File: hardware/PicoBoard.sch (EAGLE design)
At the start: 44 parts, among them J1 AVR Prog., U1 FT232RLSSOP, U10 SLIDER, U2 ATMEGA328, U3 2.5mm, U4 2.5mm, U5 2.5mm, U6 2.5mm, U7 TEMT6000, U8 LMV358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

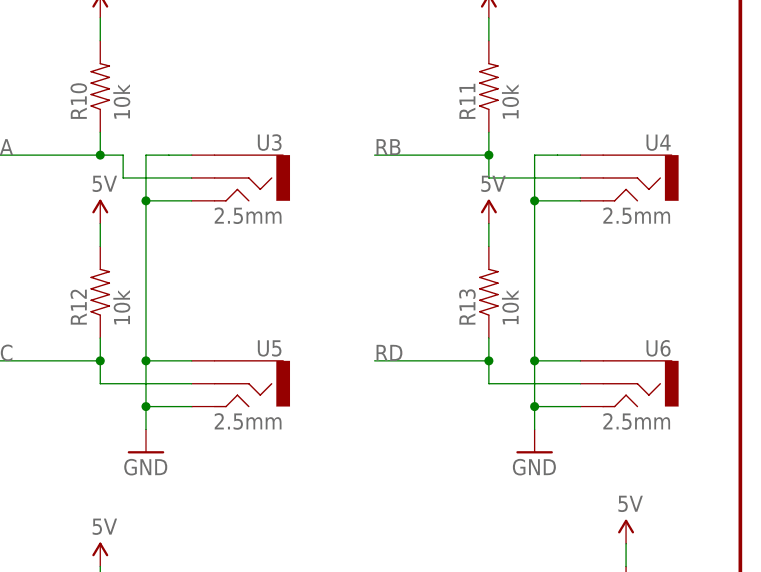
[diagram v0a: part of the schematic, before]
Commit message: Stereo Jack 1:1 updated
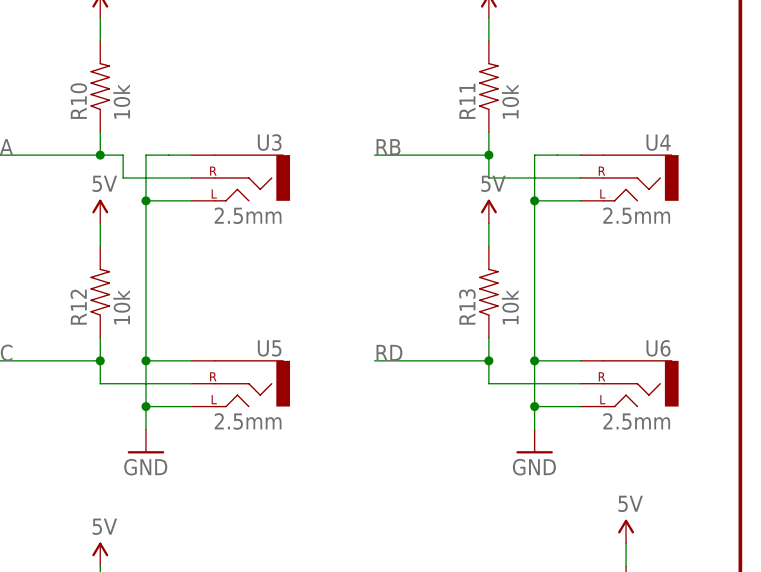
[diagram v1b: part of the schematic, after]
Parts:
- U3, U4, U5, U6: device SparkFun:AUDIO-JACKSMD -> Testing:AUDIO-JACK
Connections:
- net GND: now also U3.LEFT, U3.SLEEVE, U4.LEFT, U4.SLEEVE, U5.LEFT, U5.SLEEVE, U6.LEFT, U6.SLEEVE; no longer U3.1, U3.5, U4.1, U4.5, U5.1, U5.5, U6.1, U6.5
- net RA: now also U3.RIGHT; no longer U3.2
- net RB: now also U4.RIGHT; no longer U4.2
- net RC: now also U5.RIGHT; no longer U5.2
- net RD: now also U6.RIGHT; no longer U6.2
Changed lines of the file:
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@@
 <?xml version="1.0" encoding="utf-8"?>
 <!DOCTYPE eagle SYSTEM "eagle.dtd">
-<eagle version="6.5.0">
+<eagle version="6.4">
 <drawing>
 <settings>
@@
 <layer number="106" name="bPlate" color="7" fill="1" visible="yes" active="yes"/>
 <layer number="107" name="Crop" color="7" fill="1" visible="yes" active="yes"/>
+<layer number="108" name="tplace-old" color="10" fill="1" visible="yes" active="yes"/>
+<layer number="109" name="ref-old" color="11" fill="1" visible="yes" active="yes"/>
 <layer number="116" name="Patch_BOT" color="9" fill="4" visible="yes" active="yes"/>
 <layer number="121" name="_tsilk" color="7" fill="1" visible="yes" active="yes"/>
@@
 <part name="U$7" library="SparkFun" deviceset="5V" device=""/>
 <part name="U$8" library="SparkFun" deviceset="5V" device=""/>
-<part name="U3" library="SparkFun" deviceset="AUDIO-JACK" device="SMD" value="2.5mm"/>
-<part name="U4" library="SparkFun" deviceset="AUDIO-JACK" device="SMD" value="2.5mm"/>
-<part name="U5" library="SparkFun" deviceset="AUDIO-JACK" device="SMD" value="2.5mm"/>
-<part name="U6" library="SparkFun" deviceset="AUDIO-JACK" device="SMD" value="2.5mm"/>
+<part name="U3" library="Testing" deviceset="AUDIO-JACK" device="" value="2.5mm"/>
+<part name="U4" library="Testing" deviceset="AUDIO-JACK" device="" value="2.5mm"/>
+<part name="U5" library="Testing" deviceset="AUDIO-JACK" device="" value="2.5mm"/>
+<part name="U6" library="Testing" deviceset="AUDIO-JACK" device="" value="2.5mm"/>
 <part name="U7" library="SparkFun" deviceset="TEMT6000" device=""/>
 <part name="R4" library="SparkFun" deviceset="RESISTOR" device="0603-RES" value="100k"/>
@@
 <junction x="182.88" y="114.3"/>
 <junction x="182.88" y="96.52"/>
-<pinref part="U3" gate="G$1" pin="5"/>
-<pinref part="U5" gate="G$1" pin="5"/>
+<pinref part="U3" gate="G$1" pin="LEFT"/>
+<pinref part="U5" gate="G$1" pin="LEFT"/>
 <pinref part="GND19" gate="1" pin="GND"/>
-<pinref part="U3" gate="G$1" pin="1"/>
-<pinref part="U5" gate="G$1" pin="1"/>
+<pinref part="U3" gate="G$1" pin="SLEEVE"/>
+<pinref part="U5" gate="G$1" pin="SLEEVE"/>
 </segment>
 <segment>
@@
 <junction x="226.06" y="114.3"/>
 <junction x="226.06" y="96.52"/>
-<pinref part="U4" gate="G$1" pin="5"/>
-<pinref part="U6" gate="G$1" pin="5"/>
+<pinref part="U4" gate="G$1" pin="LEFT"/>
+<pinref part="U6" gate="G$1" pin="LEFT"/>
 <pinref part="GND20" gate="1" pin="GND"/>
-<pinref part="U4" gate="G$1" pin="1"/>
-<pinref part="U6" gate="G$1" pin="1"/>
+<pinref part="U4" gate="G$1" pin="SLEEVE"/>
+<pinref part="U6" gate="G$1" pin="SLEEVE"/>
 </segment>
 <segment>
@@
 <label x="165.1" y="119.38" size="1.778" layer="95"/>
 <pinref part="R10" gate="G$1" pin="1"/>
-<pinref part="U3" gate="G$1" pin="2"/>
+<pinref part="U3" gate="G$1" pin="RIGHT"/>
 </segment>
 </net>
@@
 <label x="208.28" y="119.38" size="1.778" layer="95"/>
 <pinref part="R11" gate="G$1" pin="1"/>
-<pinref part="U4" gate="G$1" pin="2"/>
+<pinref part="U4" gate="G$1" pin="RIGHT"/>
 </segment>
 </net>
@@
 <label x="165.1" y="96.52" size="1.778" layer="95"/>
 <pinref part="R12" gate="G$1" pin="1"/>
-<pinref part="U5" gate="G$1" pin="2"/>
+<pinref part="U5" gate="G$1" pin="RIGHT"/>
 </segment>
 </net>
@@
 <label x="208.28" y="96.52" size="1.778" layer="95"/>
 <pinref part="R13" gate="G$1" pin="1"/>
-<pinref part="U6" gate="G$1" pin="2"/>
-</segment>
-</net>
+<pinref part="U6" gate="G$1" pin="RIGHT"/>
+</segment>
+</net>

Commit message: Re- Up
95% of the orginal Rev files we're lost, updated the lost files.
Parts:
- S2: device SparkFun:SWITCH-MOMENTARY-212MM -> SparkFun-Electromechanical:SWITCH-MOMENTARY-2SMD-12MM
- U10: value SLIDER -> (none); device SparkFun:SLIDER -> SparkFun-Electromechanical:SLIDER60MM
- U3, U4, U5, U6: device Testing:AUDIO-JACK -> SparkFun-Connectors:AUDIO-JACK1:1
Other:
- note added: "Jim Lindblom"
- note added: "Revised by: Patrick Alberts"
- note added: "v12"
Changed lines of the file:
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@@
 <part name="U$7" library="SparkFun" deviceset="5V" device=""/>
 <part name="U$8" library="SparkFun" deviceset="5V" device=""/>
-<part name="U3" library="Testing" deviceset="AUDIO-JACK" device="" value="2.5mm"/>
-<part name="U4" library="Testing" deviceset="AUDIO-JACK" device="" value="2.5mm"/>
-<part name="U5" library="Testing" deviceset="AUDIO-JACK" device="" value="2.5mm"/>
-<part name="U6" library="Testing" deviceset="AUDIO-JACK" device="" value="2.5mm"/>
+<part name="U3" library="SparkFun-Connectors" deviceset="AUDIO-JACK" device="1:1" value="2.5mm"/>
+<part name="U4" library="SparkFun-Connectors" deviceset="AUDIO-JACK" device="1:1" value="2.5mm"/>
+<part name="U5" library="SparkFun-Connectors" deviceset="AUDIO-JACK" device="1:1" value="2.5mm"/>
+<part name="U6" library="SparkFun-Connectors" deviceset="AUDIO-JACK" device="1:1" value="2.5mm"/>
 <part name="U7" library="SparkFun" deviceset="TEMT6000" device=""/>
 <part name="R4" library="SparkFun" deviceset="RESISTOR" device="0603-RES" value="100k"/>
 <part name="U$10" library="SparkFun" deviceset="5V" device=""/>
 <part name="GND12" library="SparkFun" deviceset="GND" device=""/>
-<part name="S2" library="SparkFun" deviceset="SWITCH-MOMENTARY-2" device="12MM" value="12mm Button"/>
+<part name="S2" library="SparkFun-Electromechanical" deviceset="SWITCH-MOMENTARY-2" device="SMD-12MM" value="12mm Button"/>
 <part name="GND13" library="SparkFun" deviceset="GND" device=""/>
 <part name="U9" library="SparkFun" deviceset="MIC" device="9.7MM"/>
@@
 <part name="U$9" library="SparkFun" deviceset="5V" device=""/>
 <part name="U$13" library="SparkFun" deviceset="5V" device=""/>
-<part name="U10" library="SparkFun" deviceset="SLIDER" device=""/>
+<part name="U10" library="SparkFun-Electromechanical" deviceset="SLIDER" device="60MM"/>
 <part name="R10" library="SparkFun" deviceset="RESISTOR" device="0603-RES" value="10k"/>
 <part name="R11" library="SparkFun" deviceset="RESISTOR" device="0603-RES" value="10k"/>
@@
 <plain>
 <text x="200.66" y="53.34" size="1.778" layer="97" rot="MR0">LMV358</text>
+<text x="170.688" y="11.684" size="2.54" layer="94" ratio="10">Jim Lindblom</text>
+<text x="149.86" y="7.62" size="2.54" layer="94" ratio="10">Revised by: Patrick Alberts</text>
+<text x="238.76" y="7.62" size="1.778" layer="94">v12</text>
 </plain>
 <instances>

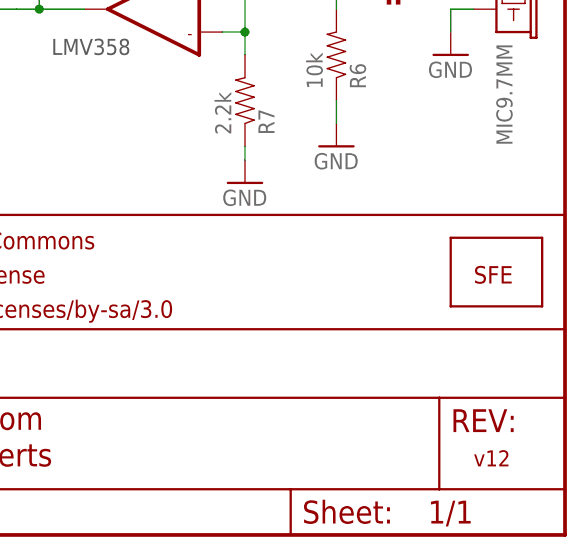
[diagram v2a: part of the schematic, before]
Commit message: Added board fiducials
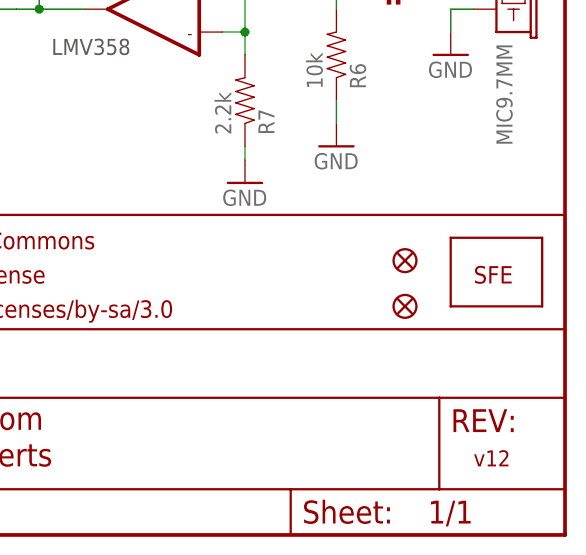
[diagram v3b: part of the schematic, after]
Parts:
- added FID1, FID2: FIDUCIAL1X2, SparkFun-Aesthetics:FIDUCIAL1X2
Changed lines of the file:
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@@
 <?xml version="1.0" encoding="utf-8"?>
 <!DOCTYPE eagle SYSTEM "eagle.dtd">
-<eagle version="6.4">
+<eagle version="6.5.0">
 <drawing>
 <settings>
@@
 <part name="FRAME1" library="SparkFun-Aesthetics" deviceset="FRAME-LETTER" device=""/>
 <part name="LOGO1" library="SparkFun-Aesthetics" deviceset="OSHW-LOGO" device="L"/>
+<part name="FID1" library="SparkFun-Aesthetics" deviceset="FIDUCIAL" device="1X2"/>
+<part name="FID2" library="SparkFun-Aesthetics" deviceset="FIDUCIAL" device="1X2"/>
 </parts>
 <sheets>
@@
 <instance part="FRAME1" gate="G$2" x="147.32" y="0"/>
 <instance part="LOGO1" gate="G$1" x="127" y="12.7"/>
+<instance part="FID1" gate="G$1" x="231.14" y="30.48"/>
+<instance part="FID2" gate="G$1" x="231.14" y="25.4"/>
 </instances>
 <busses>
